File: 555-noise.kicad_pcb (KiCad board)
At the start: 2 copper layers, 25.4 x 25.4 mm, 9 parts, among them SW1 SPST, U1 TS555CDT

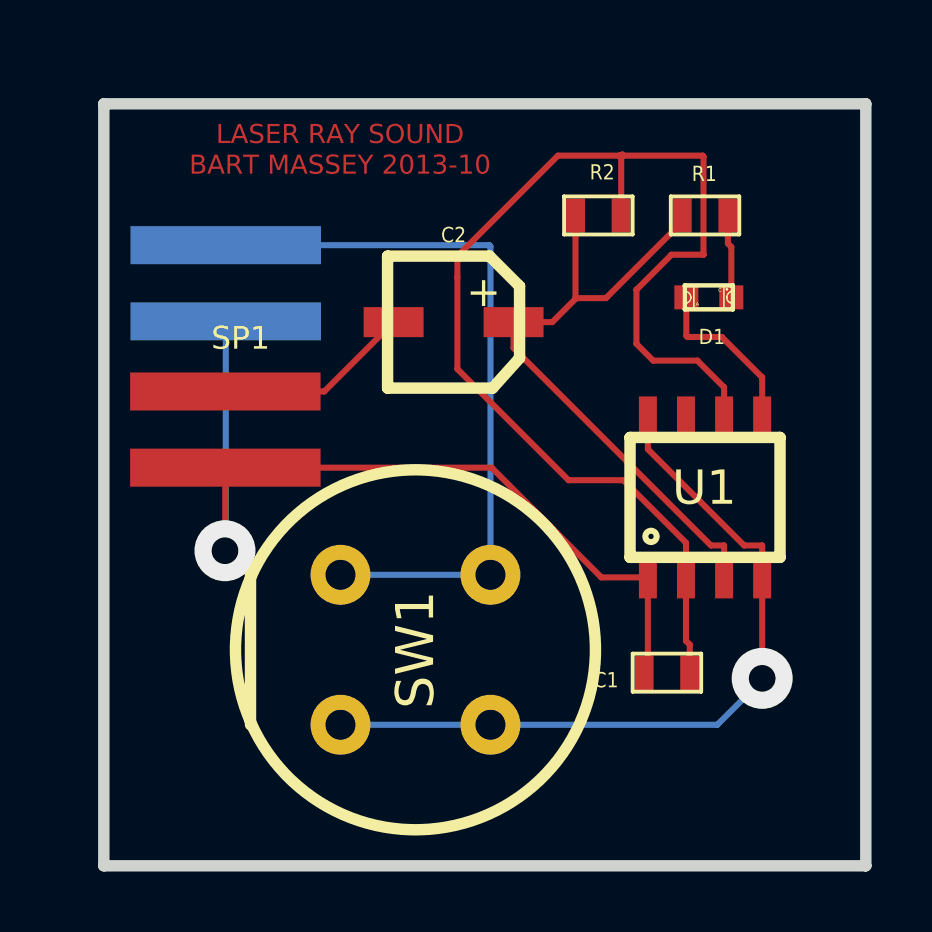
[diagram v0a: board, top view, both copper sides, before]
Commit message: updated and packaged for OSH Park; not yet ready to submit
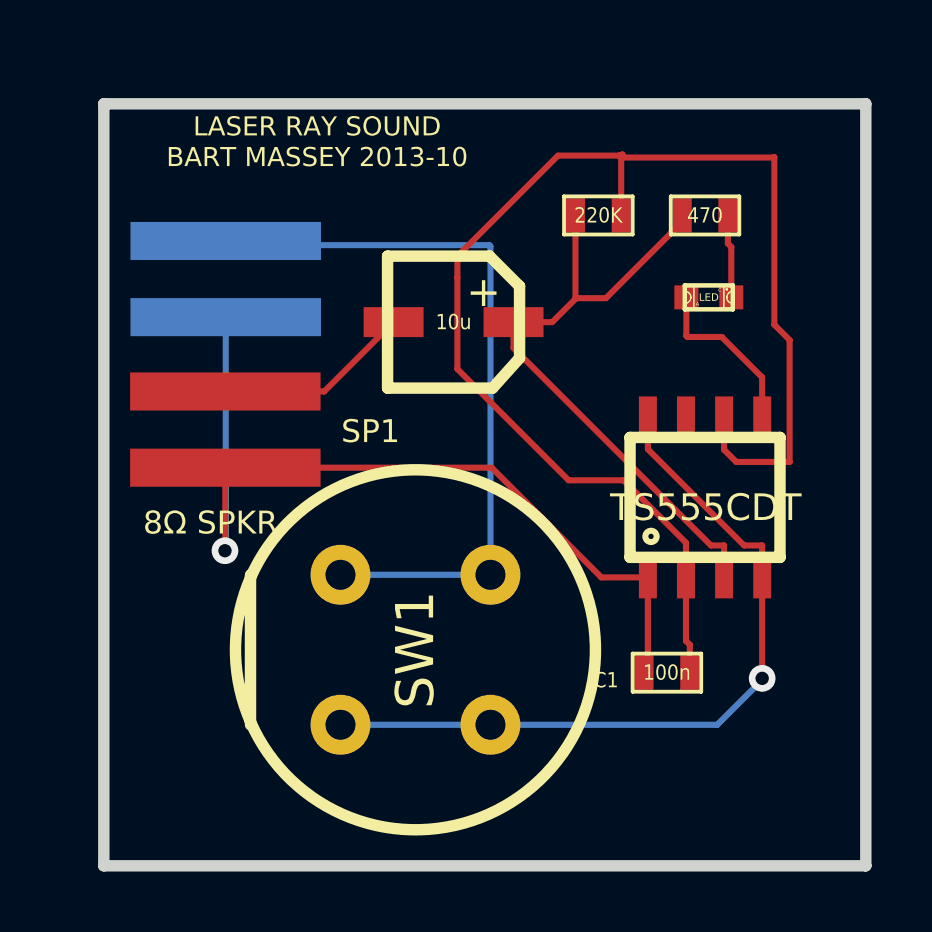
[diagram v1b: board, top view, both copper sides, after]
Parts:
- SP1: value 8ohm_SPEAKER -> 8Ω SPKR
- moved BT1 0.14 mm to (142.5, 108.7)
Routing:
- net N-000008: track 42.3 -> 46.1 mm
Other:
- rule via_min_drill: 0.254 -> 0.508
- rule via_min_size: 0.762 -> 0.889
- board text added: "+"

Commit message: version finally shipped to OSHPark
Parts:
- C2: value 10u -> 10μF
- moved BT1 1.53 mm to (141.9, 107.3)
- moved C1 1.53 mm to (159.1, 120.4)
- moved D1 1.53 mm to (160.5, 107.9)
- moved SW1 1.53 mm to (150.7, 119.7)
- moved C2 1.53 mm to (152.0, 108.8)
- moved R1 1.53 mm to (160.4, 105.2)
- moved U1 1.53 mm to (160.4, 114.6)
- moved R2 1.53 mm to (156.8, 105.2)
- moved SP1 1.53 mm to (146.9, 112.3)
